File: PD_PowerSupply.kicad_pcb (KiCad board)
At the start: 2 copper layers, 83 x 42 mm, 79 parts, among them J1 Connector, J2 Connector, J3 Connector, J4 Connector, Q1 STL6P3LLH6, Q2 STL6P3LLH6, Q3 MMBT3906, Q4 MMBT3906, U1 nRF52840, U2 STUSB4500QTR, U3 STM32L432KCUx, U4 LTM8074IY#PBF, U5 LTC2972, U6 LTM8074IY#PBF, U7 LTM8074IY#PBF

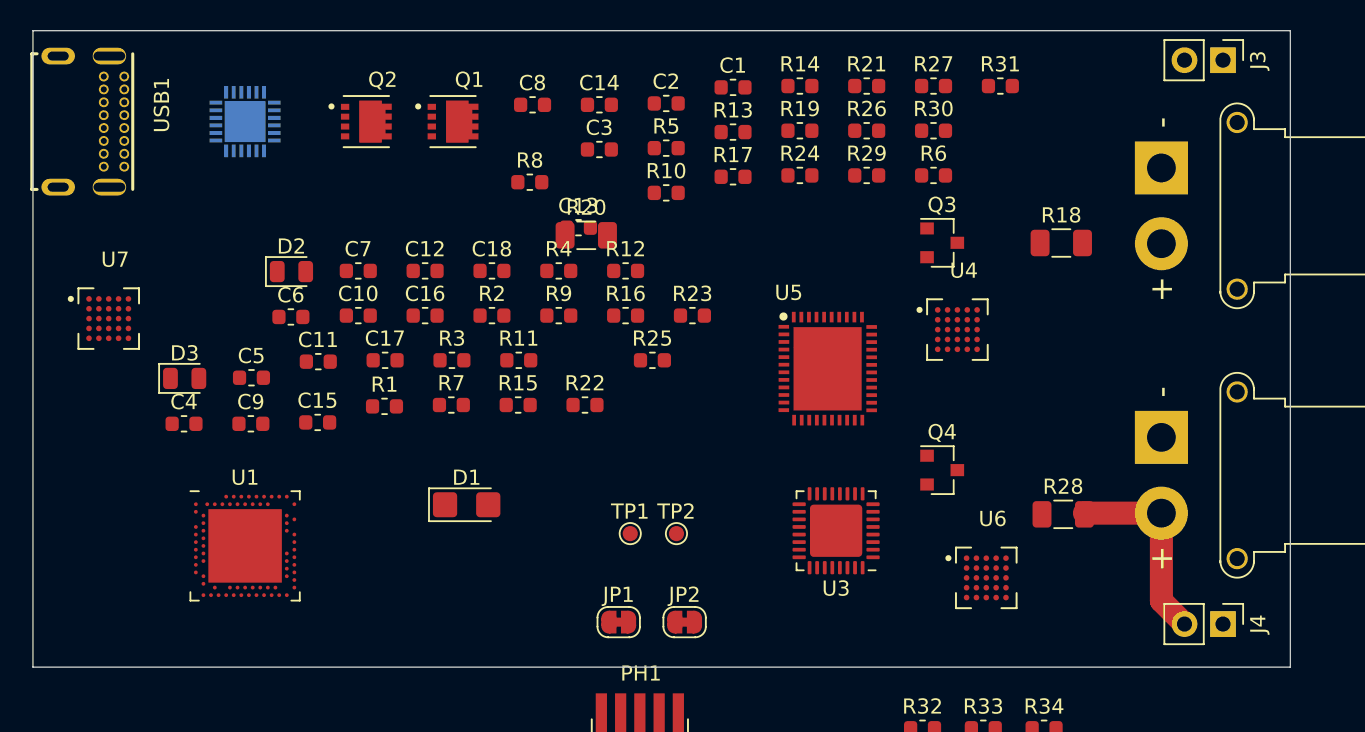
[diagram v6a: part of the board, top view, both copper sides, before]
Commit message: added secondary 2.54 headers
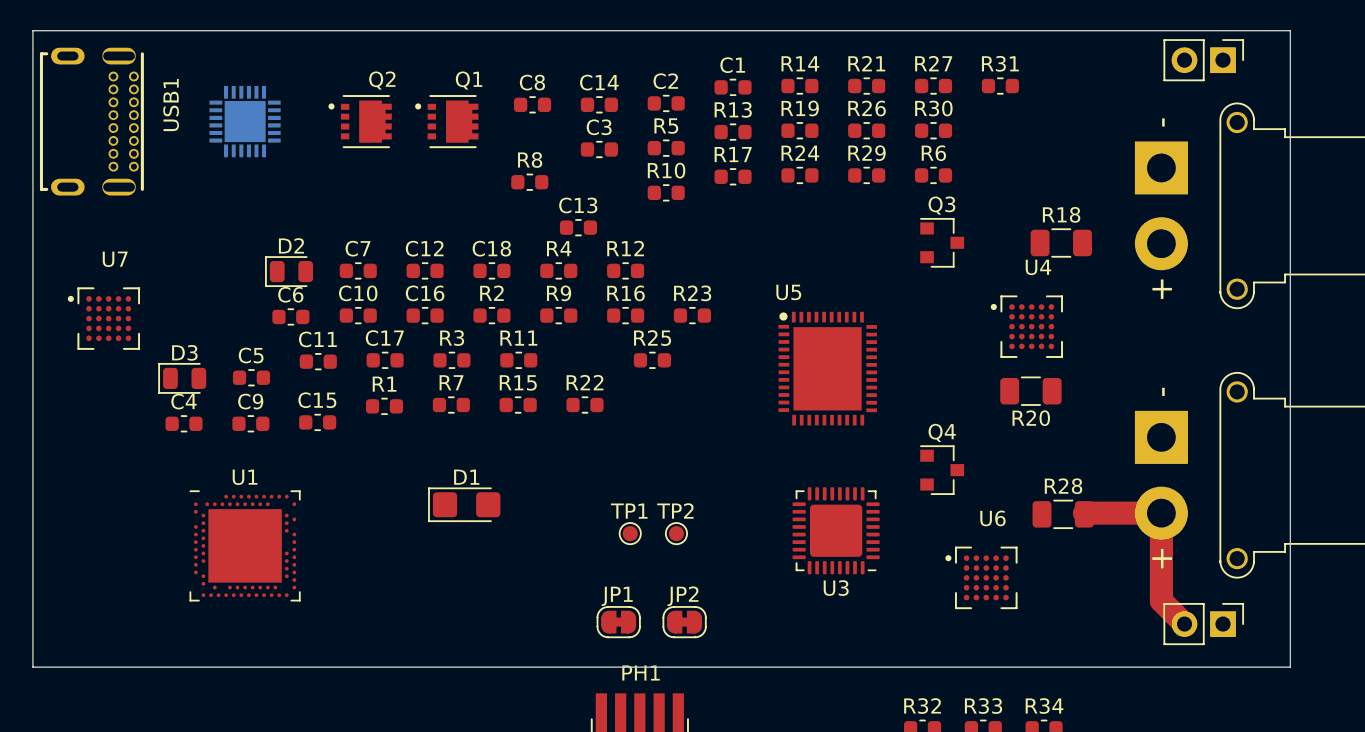
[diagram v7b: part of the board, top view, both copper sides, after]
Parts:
- moved R20 31.1 mm to (179.9, 97.8), turned to 180 degrees
- moved U4 4.91 mm to (179.9, 93.5)
- moved USB1 0.64 mm to (116.6, 80.0)
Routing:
- added copper zone on In2.Cu, net +3V3
- added copper zone on In1.Cu, net GND
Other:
- copper layers 2 -> 4
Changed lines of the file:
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@@
   (layers
     (0 F.Cu signal)
+    (1 In1.Cu power hide)
+    (2 In2.Cu power hide)
     (31 B.Cu signal)
     (32 B.Adhes user)
@@
   )
   (setup
-    (last_trace_width 1.524)
+    (last_trace_width 0.254)
     (user_trace_width 0.254)
     (user_trace_width 0.508)
@@
     (pcb_text_width 0.3)
     (pcb_text_size 1.5 1.5)
-    (mod_edge_width 0.12)
+    (mod_edge_width 0.065)
     (mod_text_size 1 1)
     (mod_text_width 0.15)
@@
     (descr "Through hole straight pin header, 1x02, 2.54mm pitch, single row")
     (tags "Through hole pin header THT 1x02 2.54mm single row")
-    (fp_text reference J4 (at 0 -2.33 90) (layer F.SilkS)
+    (fp_text reference J4 (at 0 -2.33 90) (layer F.SilkS) hide
       (effects (font (size 1 1) (thickness 0.15)))
     )
-    (fp_text value Connector (at 0 4.87 90) (layer F.Fab)
+    (fp_text value Connector (at 3.7846 1.143) (layer F.Fab)
       (effects (font (size 1 1) (thickness 0.15)))
     )
@@
     (descr "Through hole straight pin header, 1x02, 2.54mm pitch, single row")
     (tags "Through hole pin header THT 1x02 2.54mm single row")
-    (fp_text reference J3 (at 0 -2.33 90) (layer F.SilkS)
+    (fp_text reference J3 (at 0 -2.33 90) (layer F.SilkS) hide
       (effects (font (size 1 1) (thickness 0.15)))
     )
-    (fp_text value Connector (at 0 4.87 90) (layer F.Fab)
+    (fp_text value Connector (at -2.794 0.889 180) (layer F.Fab)
       (effects (font (size 1 1) (thickness 0.15)))
     )
@@
   )
   (module Resistor_SMD:R_1206_3216Metric (layer F.Cu)
-    (at 150.514001 87.505001)
+    (at 179.8574 97.79 180)
     (descr "Resistor SMD 1206 (3216 Metric), square (rectangular) end terminal, IPC_7351 nominal, (Body size source: http://www.tortai-tech.com/upload/download/2011102023233369053.pdf), generated with kicad-footprint-generator")
     (tags resistor)
@@
     (fp_line (start -1.6 -0.8) (end 1.6 -0.8) (layer F.Fab) (width 0.1))
     (fp_line (start -1.6 0.8) (end -1.6 -0.8) (layer F.Fab) (width 0.1))
-    (pad 2 smd roundrect (at 1.4 0) (size 1.25 1.75) (layers F.Cu F.Paste F.Mask) (roundrect_rratio 0.2)
+    (pad 2 smd roundrect (at 1.4 0 180) (size 1.25 1.75) (layers F.Cu F.Paste F.Mask) (roundrect_rratio 0.2)
       (net 10 VBUS))
-    (pad 1 smd roundrect (at -1.4 0) (size 1.25 1.75) (layers F.Cu F.Paste F.Mask) (roundrect_rratio 0.2)
+    (pad 1 smd roundrect (at -1.4 0 180) (size 1.25 1.75) (layers F.Cu F.Paste F.Mask) (roundrect_rratio 0.2)
       (net 11 /vSINK))
     (model ${KISYS3DMOD}/Resistor_SMD.3dshapes/R_1206_3216Metric.wrl
@@
       (effects (font (size 1 1) (thickness 0.15)))
     )
-    (fp_text value Connector (at 2.5 3.5 90) (layer F.Fab)
+    (fp_text value Connector (at 2.286 -7.0104 90) (layer F.Fab)
       (effects (font (size 1 1) (thickness 0.15)))
     )
@@
       (effects (font (size 1 1) (thickness 0.15)))
     )
-    (fp_text value Connector (at 2.5 3.5 90) (layer F.Fab)
+    (fp_text value Connector (at 2.5654 -7.112 90) (layer F.Fab)
       (effects (font (size 1 1) (thickness 0.15)))
     )
@@
   )
   (module USB4085-GF-A_REVA:GCT_USB4085-GF-A_REVA (layer F.Cu)
-    (at 116 80 270)
+    (at 116.6368 80 270)
     (fp_text reference USB1 (at -1.097425 -6.515415 90) (layer F.SilkS)
       (effects (font (size 1.00015 1.00015) (thickness 0.015)))
@@
   )
   (module LTM8074IY_PBF:BGA25C65P5X5_400X400X198N (layer F.Cu)
-    (at 175.006 93.726)
+    (at 179.9082 93.5332)
     (fp_text reference U4 (at 0.425 -3.885) (layer F.SilkS)
       (effects (font (size 1 1) (thickness 0.015)))
@@
   (segment (start 188.468 111.633) (end 189.992 113.157) (width 1.524) (layer F.Cu) (net 153))
   (segment (start 188.468 105.838) (end 188.468 111.633) (width 1.524) (layer F.Cu) (net 153))
+  (zone (net 3) (net_name GND) (layer In1.Cu) (hatch edge 0.508)
+    (connect_pads (clearance 0.508))
+    (min_thickness 0.254)
+    (fill yes (arc_segments 32) (thermal_gap 0.508) (thermal_bridge_width 0.508))
+    (polygon
+      (pts
+        (xy 199.21855 117.0432) (xy 113.644363 116.99875) (xy 113.482438 73.50125) (xy 199.056625 73.5457)
+      )
+    )
+  )
+  (zone (net 14) (net_name +3V3) (layer In2.Cu) (hatch edge 0.508)
+    (connect_pads (clearance 0.508))
+    (min_thickness 0.254)
+    (fill yes (arc_segments 32) (thermal_gap 0.508) (thermal_bridge_width 0.508))
+    (polygon
+      (pts
+        (xy 204.597 119.0244) (xy 108.6612 119.0244) (xy 108.6612 70.3834) (xy 204.597 70.3834)
+      )
+    )
+  )
 )

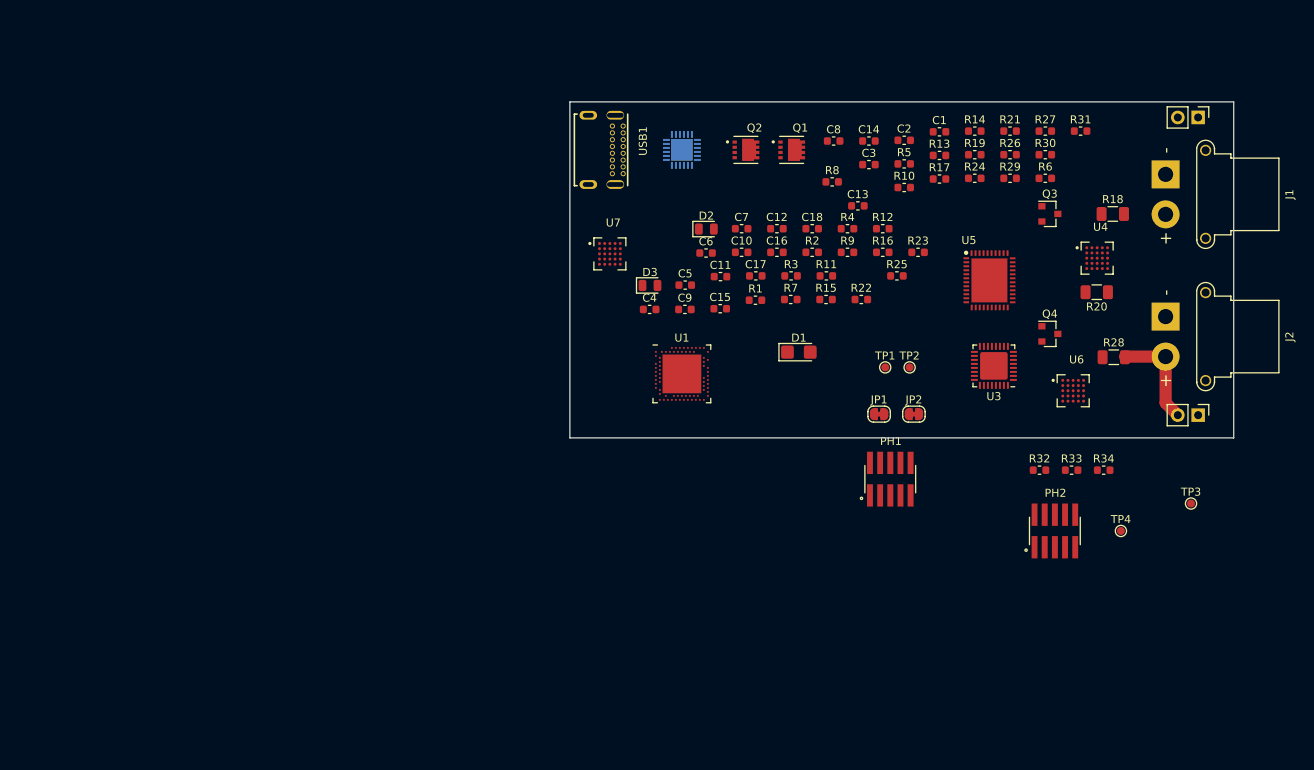
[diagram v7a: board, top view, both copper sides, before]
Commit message: started routing switchers
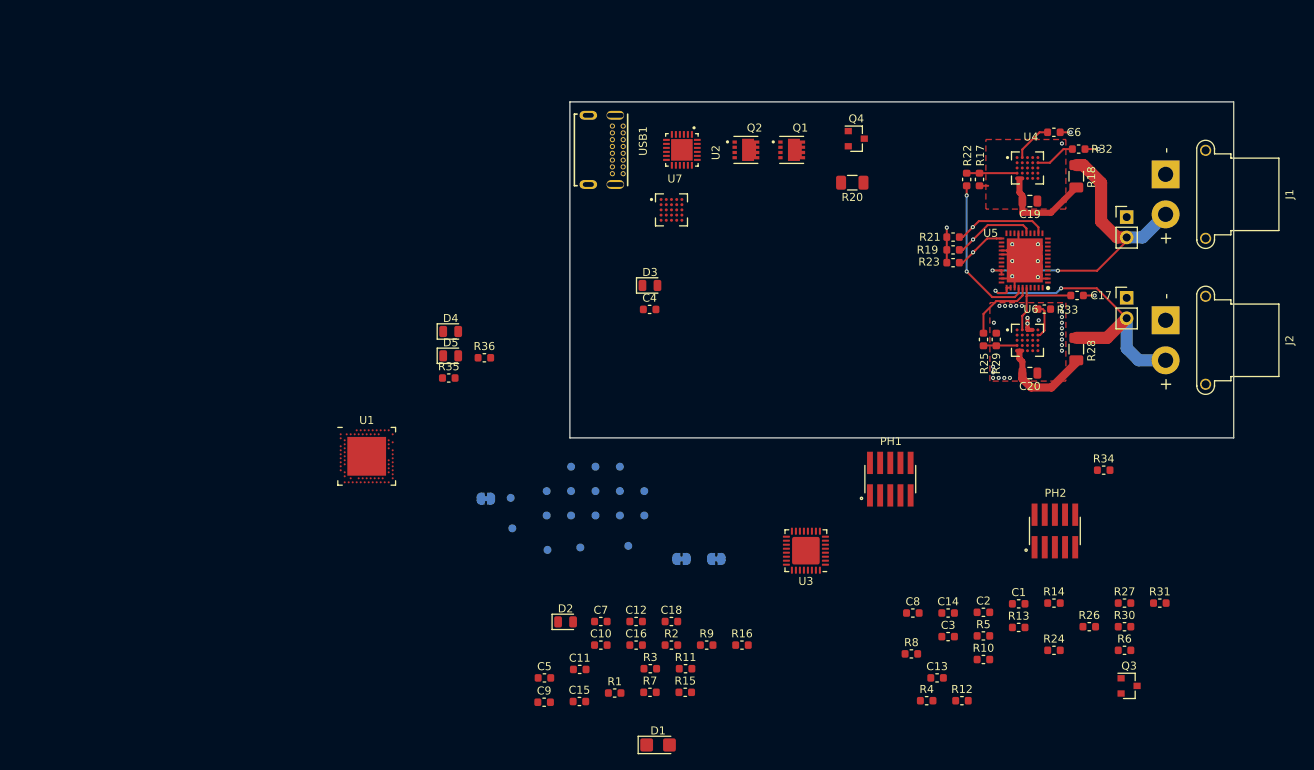
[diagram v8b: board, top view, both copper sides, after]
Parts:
- added +3V3: TestPoint, TestPoint:TestPoint_Pad_D1.0mm, B.Cu at (111.1, 125.7)
- added C19: 10uF, Capacitor_SMD:C_0805_2012Metric, F.Cu at (171.5, 86.4)
- added C20: 10uF, Capacitor_SMD:C_0805_2012Metric, F.Cu at (171.5, 107.9)
- added D4: BLUE 0805, LED_SMD:LED_0805_2012Metric, F.Cu at (99.1, 102.7)
- added D5: ORANGE 0805, LED_SMD:LED_0805_2012Metric, F.Cu at (99.1, 105.7)
- added GND1: TestPoint, TestPoint:TestPoint_Pad_D1.0mm, B.Cu at (111.1, 122.7)
- added I2C_SCL1: TestPoint, TestPoint:TestPoint_Pad_D1.0mm, B.Cu at (114.2, 125.7)
- added I2C_SDA1: TestPoint, TestPoint:TestPoint_Pad_D1.0mm, B.Cu at (111.2, 130.0)
- added JP3: SolderJumper_2_Bridged, Jumper:SolderJumper-2_P1.3mm_Bridged_RoundedPad1.0x1.5mm, B.Cu at (103.5, 123.6)
- added P0.13: TestPoint, TestPoint:TestPoint_Pad_D1.0mm, B.Cu at (114.2, 119.6)
- added P0.14: TestPoint, TestPoint:TestPoint_Pad_D1.0mm, B.Cu at (117.2, 125.7)
- added P0.15: TestPoint, TestPoint:TestPoint_Pad_D1.0mm, B.Cu at (117.2, 119.6)
- added P0.16: TestPoint, TestPoint:TestPoint_Pad_D1.0mm, B.Cu at (114.2, 122.7)
- added P0.17: TestPoint, TestPoint:TestPoint_Pad_D1.0mm, B.Cu at (117.2, 122.7)
- added P0.19: TestPoint, TestPoint:TestPoint_Pad_D1.0mm, B.Cu at (123.3, 125.7)
- added P0.20: TestPoint, TestPoint:TestPoint_Pad_D1.0mm, B.Cu at (120.2, 122.7)
- added P0.21: TestPoint, TestPoint:TestPoint_Pad_D1.0mm, B.Cu at (120.2, 125.7)
- added PMB_SCL1: TestPoint, TestPoint:TestPoint_Pad_D1.0mm, B.Cu at (120.2, 119.6)
- added PMB_SDA1: TestPoint, TestPoint:TestPoint_Pad_D1.0mm, B.Cu at (123.3, 122.7)
- added R35: 300, Resistor_SMD:R_0603_1608Metric, F.Cu at (98.9, 108.5)
- added R36: 300, Resistor_SMD:R_0603_1608Metric, F.Cu at (103.3, 106.0)
- JP1, JP2, TP1, TP2, TP3, TP4: moved to B.Cu
- U2: moved to F.Cu
- moved TP3 70.5 mm to (121.3, 129.5)
- moved TP4 67.6 mm to (115.3, 129.7)
- moved C3 59.8 mm to (161.3, 140.8)
- moved R13 59.8 mm to (170.1, 139.7)
- moved R5 59.8 mm to (165.7, 140.8)
- moved C13 59.8 mm to (159.9, 146.0)
- moved C14 59.8 mm to (161.3, 137.9)
- moved C8 59.8 mm to (156.9, 137.9)
- moved Q3 59.8 mm to (183.9, 147.0)
- moved R10 59.8 mm to (165.7, 143.7)
- moved R30 59.8 mm to (183.3, 139.6)
- moved R4 59.8 mm to (158.6, 148.9)
- moved R8 59.8 mm to (156.7, 143.0)
- moved R12 59.8 mm to (163.0, 148.9)
- moved R26 59.8 mm to (178.9, 139.6)
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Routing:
- net Net-(J1-Pad2): track 0.00 -> 39.4 mm, vias 0 -> 2
- net GND: track 0.00 -> 27.7 mm, vias 0 -> 25
- net Net-(J2-Pad2): track 13.1 -> 37.5 mm, vias 0 -> 2
- net Net-(R22-Pad2): track 0.00 -> 19.4 mm, vias 0 -> 2
- net Net-(C20-Pad2): track 0.00 -> 13.0 mm
- net Net-(C19-Pad2): track 0.00 -> 12.9 mm
- net Net-(R21-Pad2): track 0.00 -> 11.8 mm, vias 0 -> 1
- net Net-(C17-Pad2): track 0.00 -> 11.1 mm
- net /FAULTB0: track 0.00 -> 10.4 mm, vias 0 -> 1
- net Net-(R25-Pad2): track 0.00 -> 9.24 mm
- net /CONTROL0: track 0.00 -> 6.52 mm, vias 0 -> 1
- net Net-(R17-Pad1): track 0.00 -> 6.30 mm
- net Net-(C6-Pad2): track 0.00 -> 5.06 mm
- net Net-(R32-Pad1): track 0.00 -> 5.02 mm
- net Net-(R33-Pad1): track 0.00 -> 4.42 mm
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- added copper zone on F.Cu, net GND
